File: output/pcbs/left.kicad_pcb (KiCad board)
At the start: 2 copper layers, 138 x 108.2 mm, 0 parts

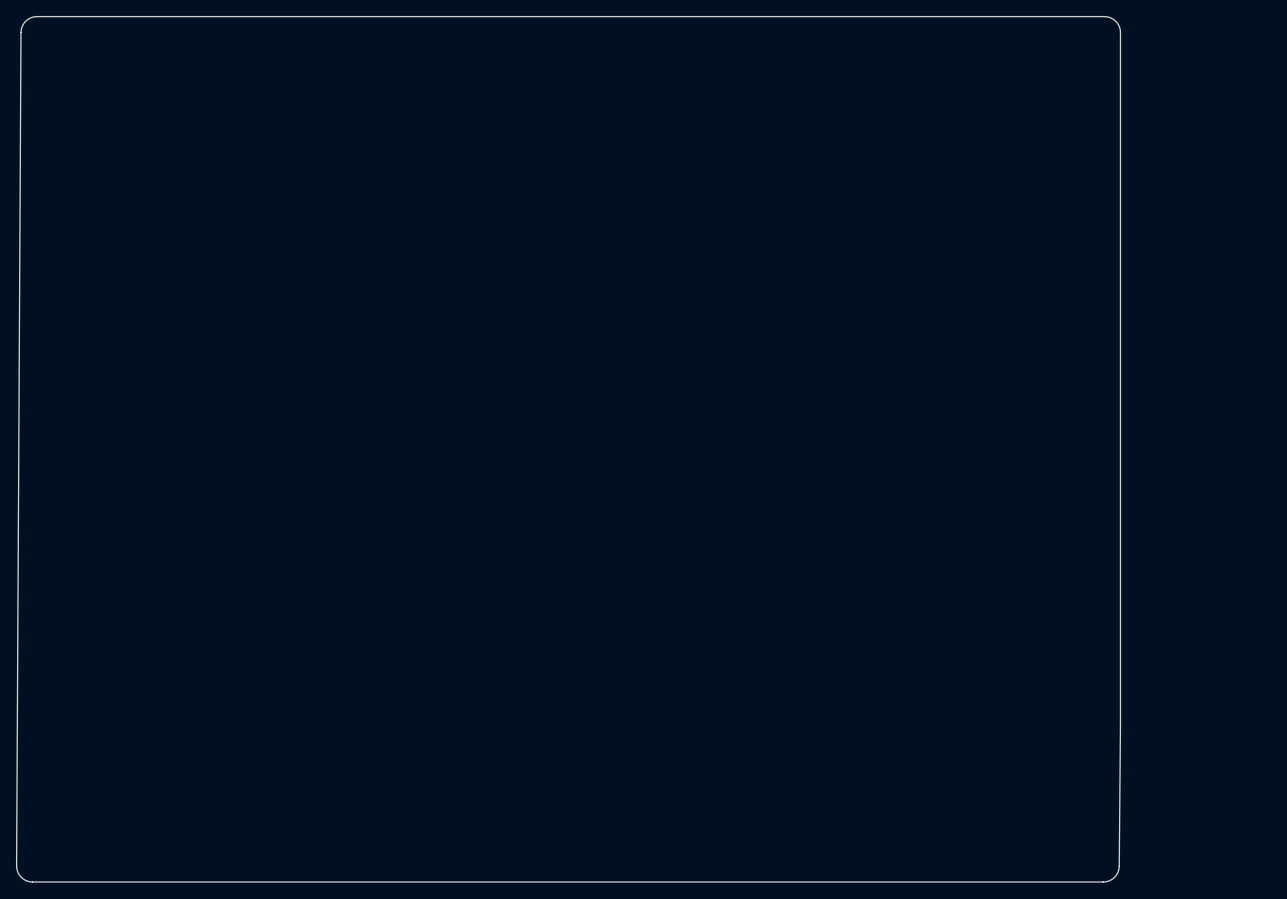
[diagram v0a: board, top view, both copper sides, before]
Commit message: trying to place ts, not working. hotswap not showing up
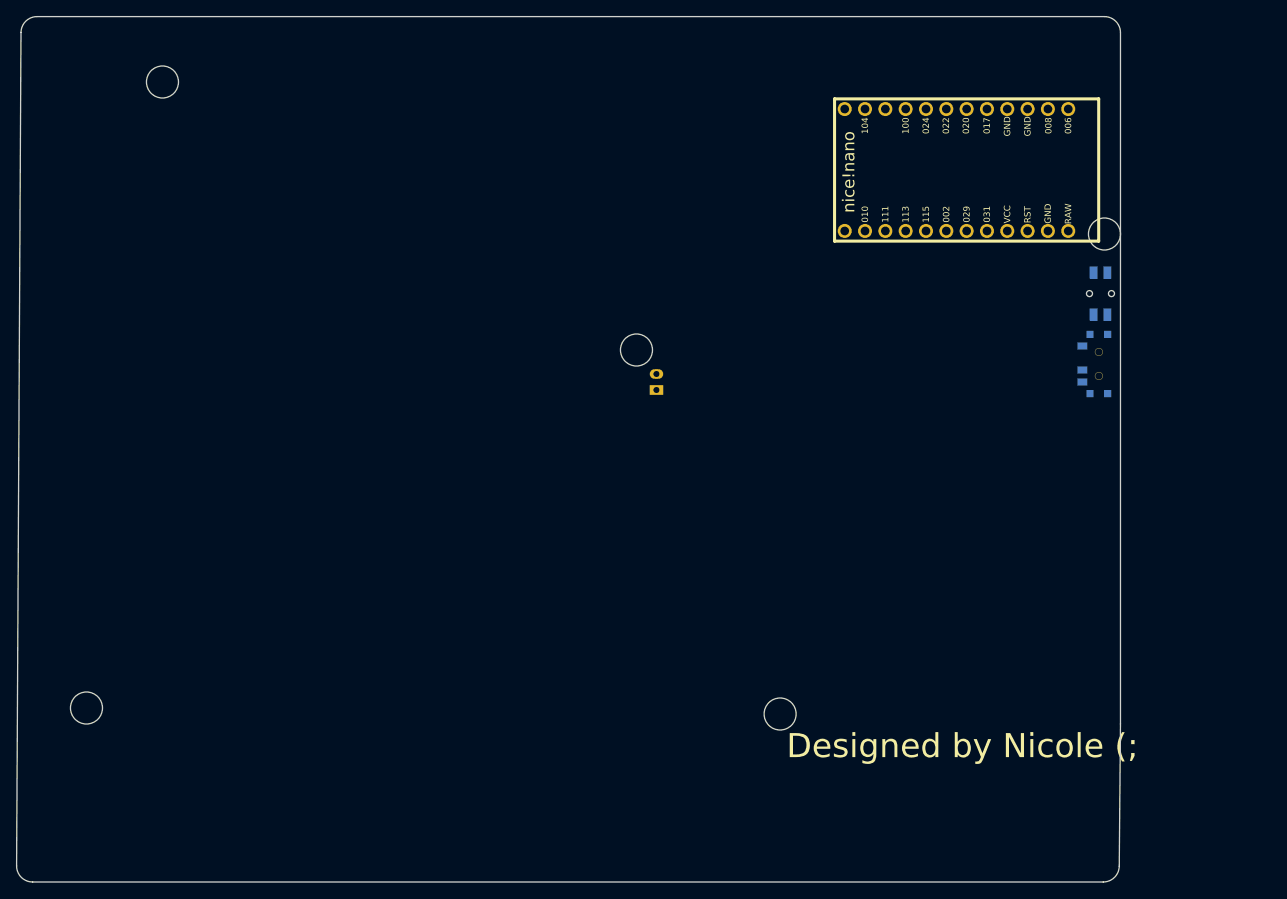
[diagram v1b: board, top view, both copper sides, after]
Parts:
- added ?: , HOLE_M2_TH, F.Cu at (-29.2, -68.8)
- added ?: , HOLE_M2_TH, F.Cu at (88.5, -49.8)
- added ?: , HOLE_M2_TH, F.Cu at (-38.8, 9.50)
- added ?: , HOLE_M2_TH, F.Cu at (48.0, 10.2)
- added ?: , HOLE_M2_TH, F.Cu at (30.0, -35.2)
- added B1: Panasonic_EVQPUL_EVQPUC, Panasonic_EVQPUL_EVQPUC, F.Cu at (88.0, -42.3)
- added JST1: , JST_PH_S2B-PH-K_02x2.00mm_Angled, F.Cu at (32.5, -31.2)
- added MCU1: nice_nano, nice_nano, F.Cu at (70.0, -57.8)
- added T1: , E73:SPDT_C128955, F.Cu at (87.8, -33.5)
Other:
- board text added: "Designed by Nicole (;"
